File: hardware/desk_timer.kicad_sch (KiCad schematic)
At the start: 13 parts, among them SW1 SW_Push, U3 STM32G0B1CBTx, Y1 32.768 KHz, Y2 8 MHz, 10ppm

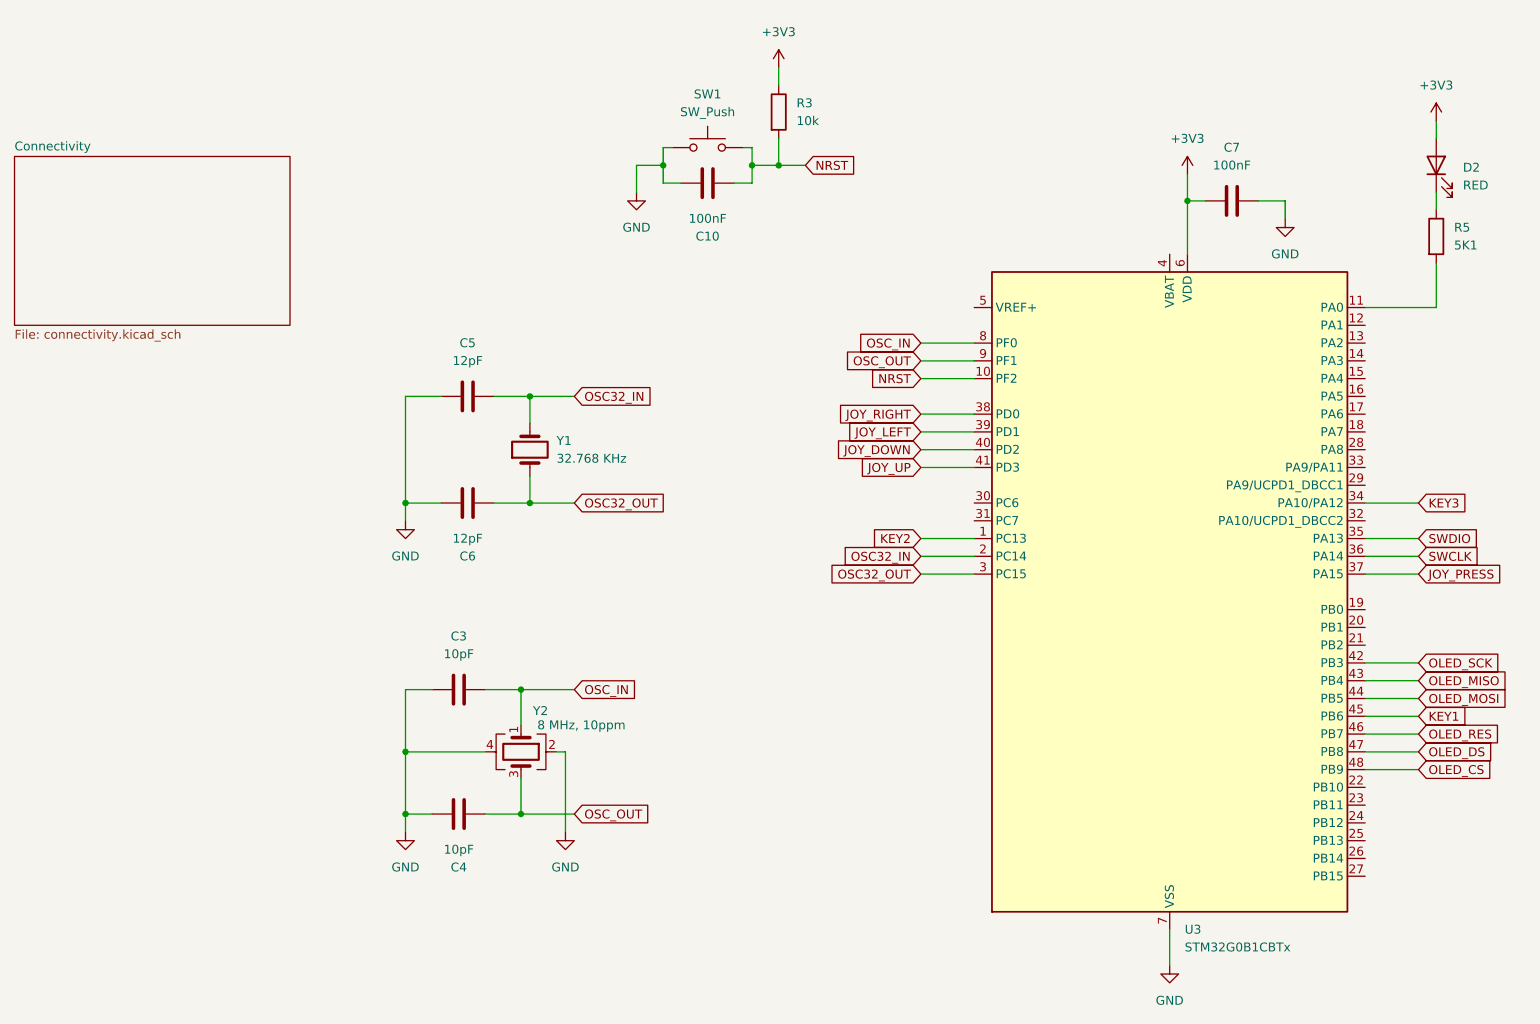
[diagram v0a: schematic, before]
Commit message: Switched to STM32G0B1, improved usage reporting, etc
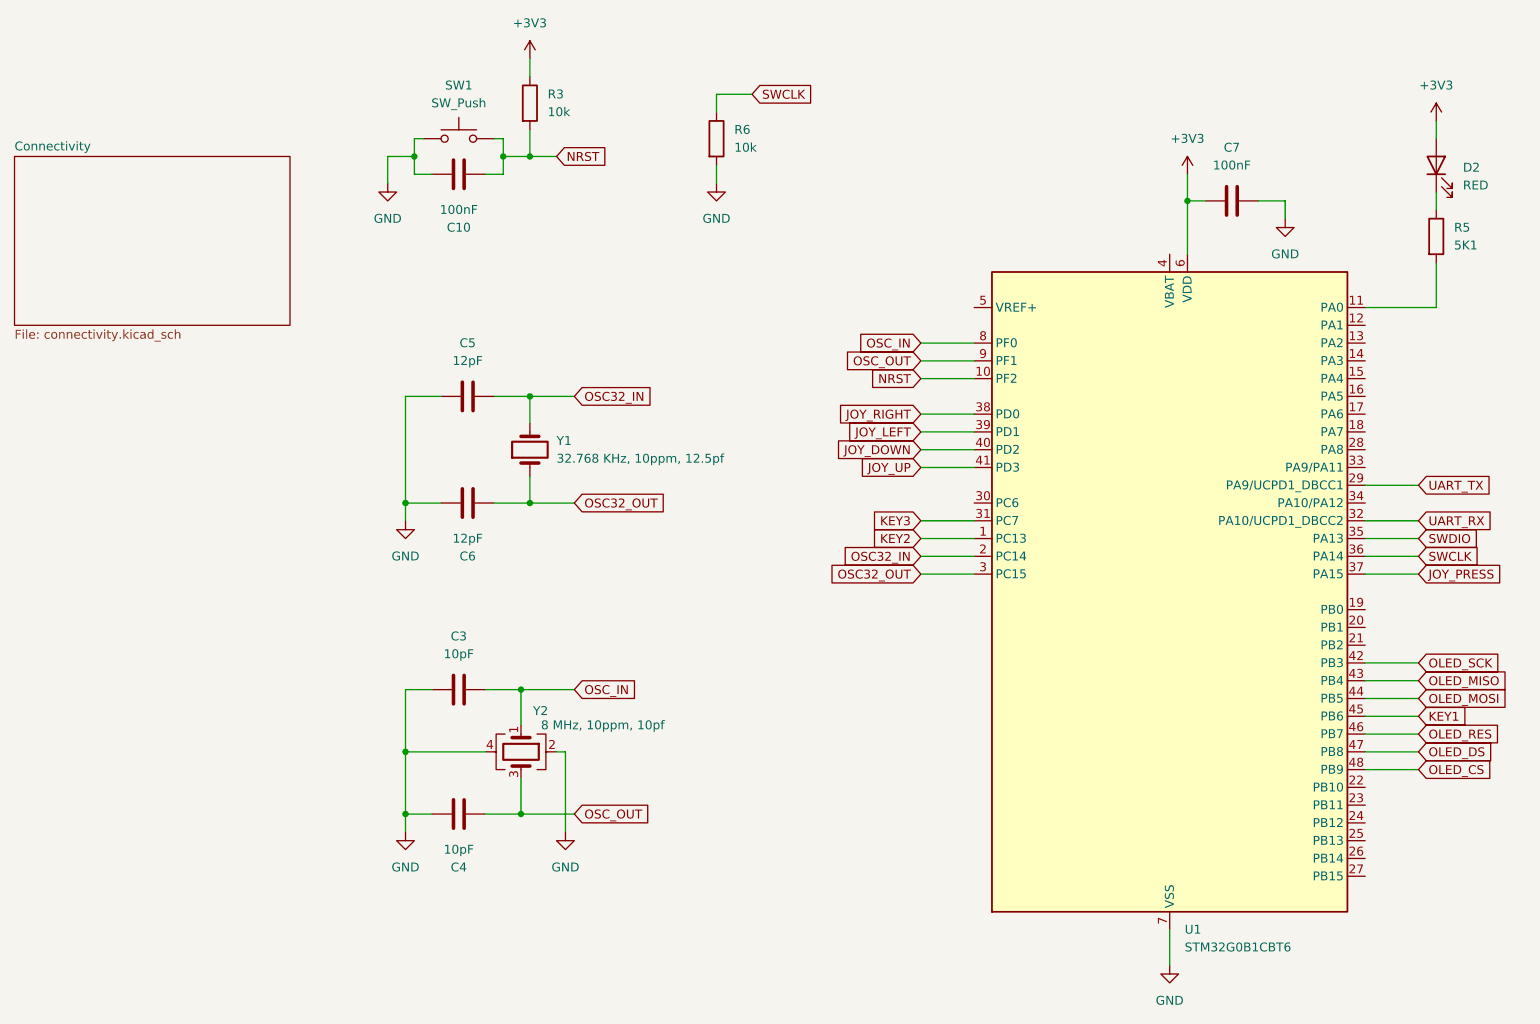
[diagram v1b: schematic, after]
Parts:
- added R6: 10k, Resistor_SMD:R_0402_1005Metric, symbol Device:R
- U1: renamed from U3; value STM32G0B1CBTx -> STM32G0B1CBT6
- Y1: value 32.768 KHz -> 32.768 KHz, 10ppm, 12.5pf
- Y2: value 8 MHz, 10ppm -> 8 MHz, 10ppm, 10pf
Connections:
- net GND: now also R6.2
- net KEY3: now also U1.31 (PC7); no longer U1.34 (PA10/PA12)
- net SWCLK: now also R6.1
- net UART_TX: now reaches U1.29 (PA9/UCPD1_DBCC1)
- net UART_RX: now reaches U1.32 (PA10/UCPD1_DBCC2)
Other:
- moved on the sheet: C10, R3, SW1
